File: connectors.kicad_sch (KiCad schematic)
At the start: 21 parts, among them J2 52746-1271, J4 SS5-10-3.00-L-D-K-TR, J8 2, M1 MountingHole_Pad, M2 MountingHole_Pad, M3 MountingHole_Pad, M4 MountingHole_Pad, U13 TXB0104RUT, U2 TXB0104RUT

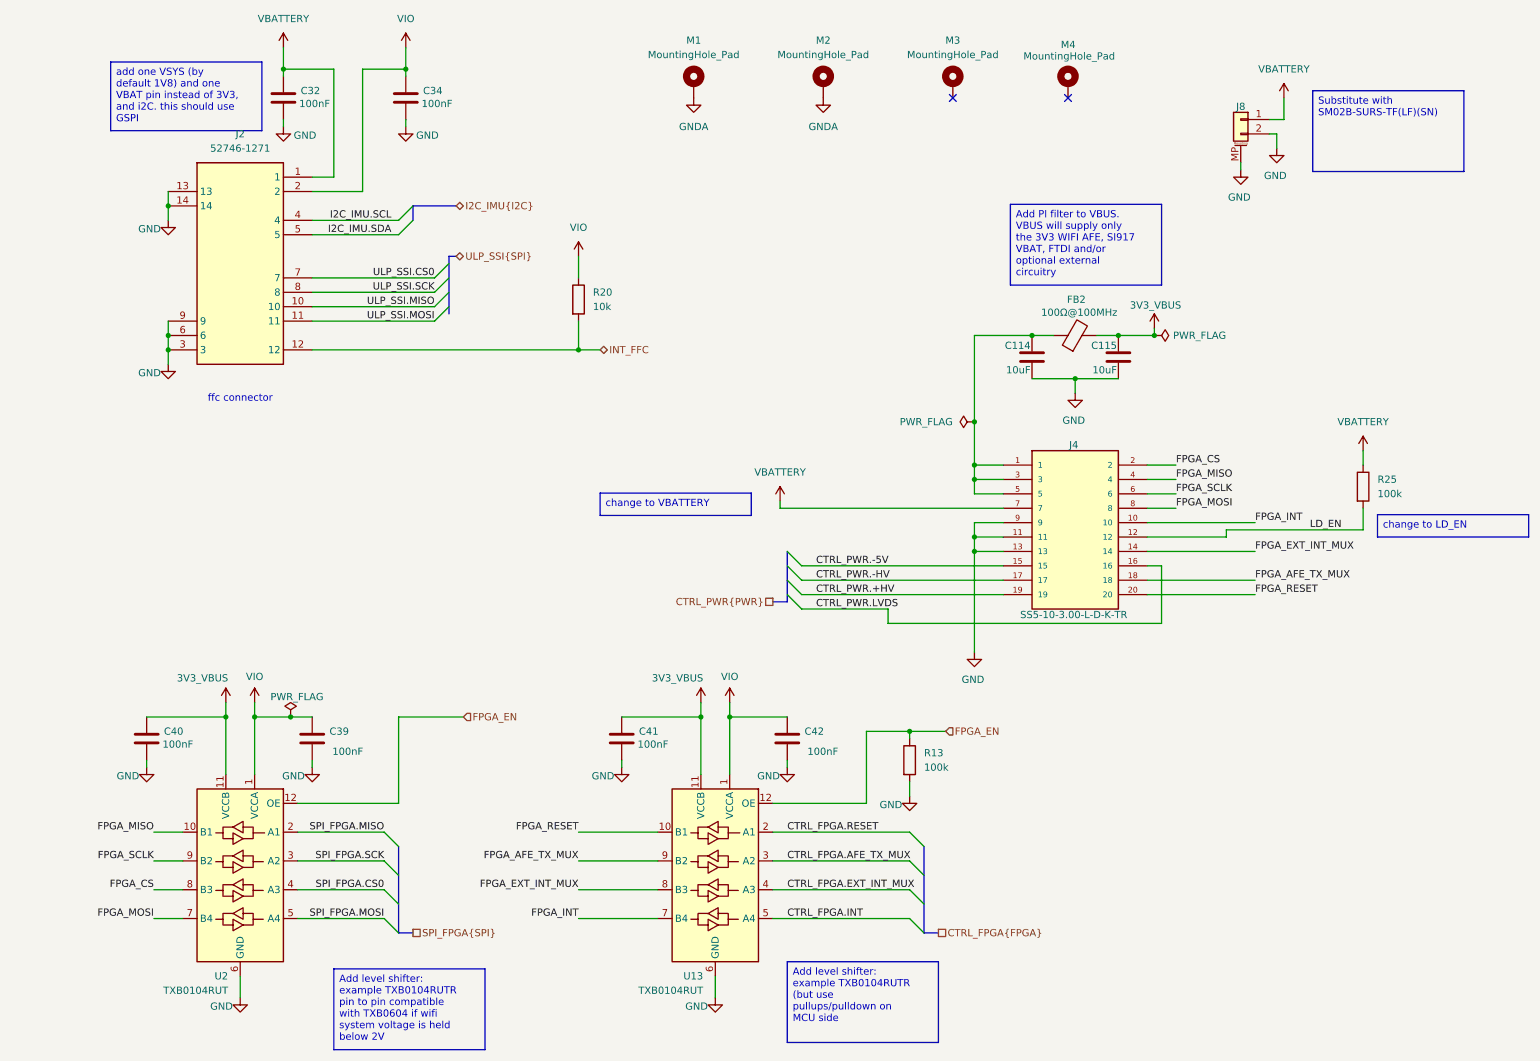
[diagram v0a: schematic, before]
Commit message: new debug connector SOICbite, new board shape, new placement, addition of 22 ohm resistance in fast digital signals as spi
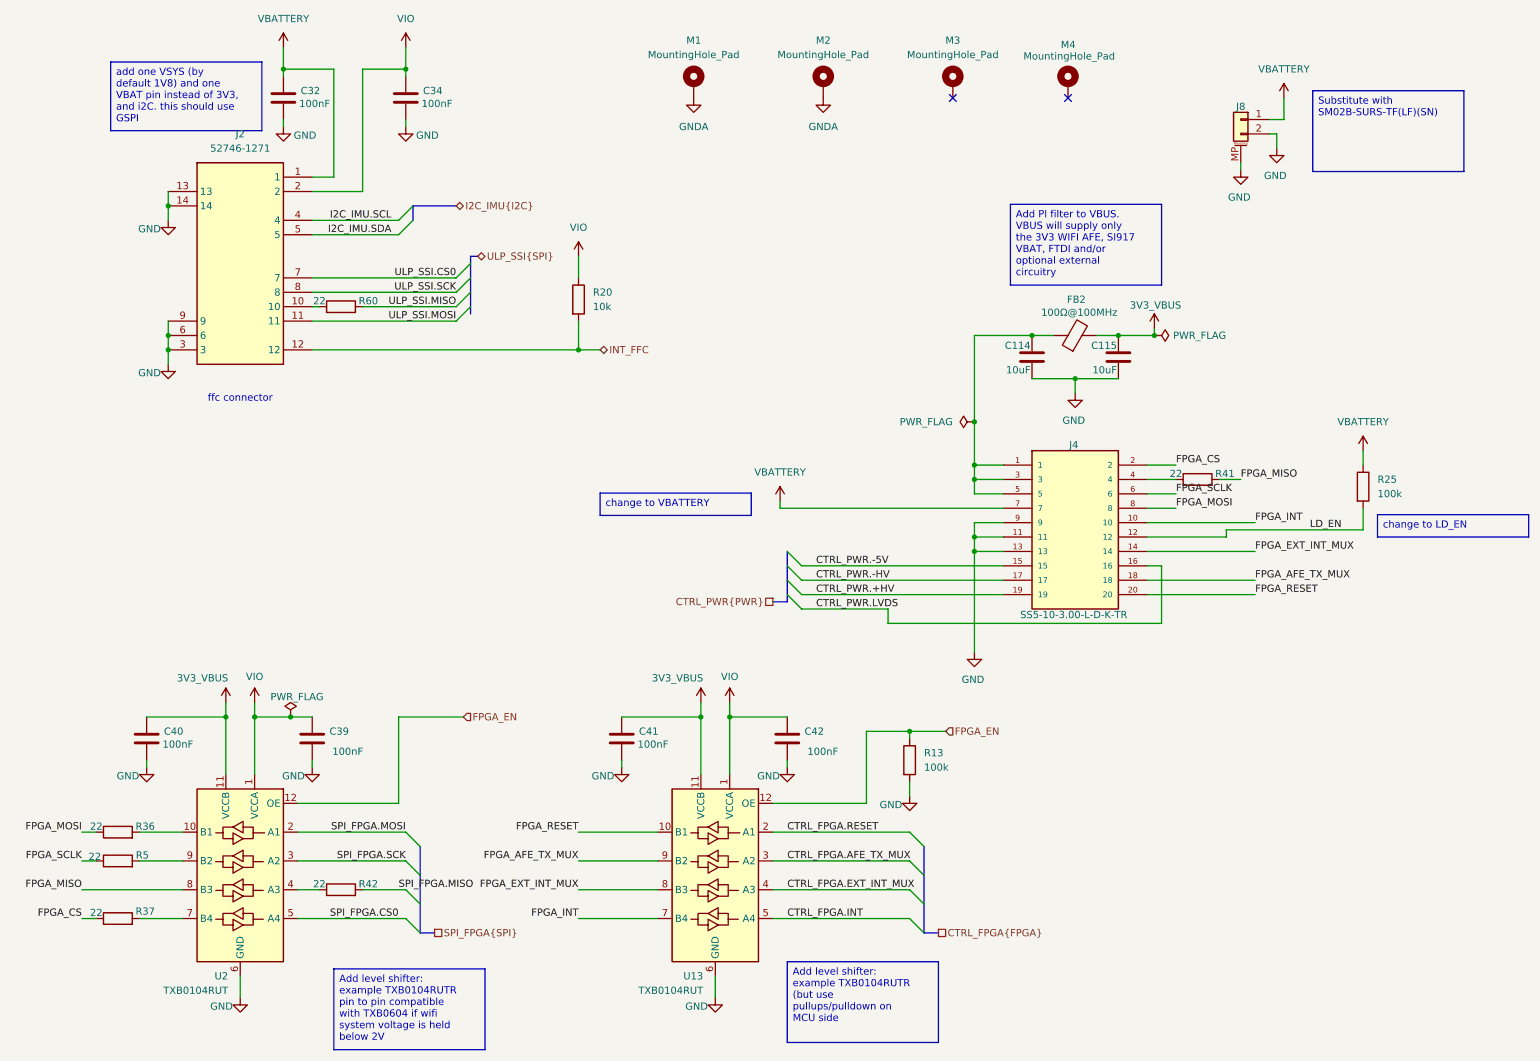
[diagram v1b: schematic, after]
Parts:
- added R36, R37, R41, R42, R5, R60: 22, Resistor_SMD:R_0201_0603Metric, symbol #dzdb:g_res/R-22-0201
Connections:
- net FPGA_CS: now also R37.1; no longer U2.8 (B3)
- net FPGA_MISO: now also U2.8 (B3), R41.2; no longer J4.4, U2.10 (B1)
- net FPGA_MOSI: now also R36.1; no longer U2.7 (B4)
- net FPGA_SCLK: now also R5.1; no longer U2.9 (B2)
- net SPI_FPGA.CS0: now also U2.5 (A4); no longer U2.4 (A3)
- net SPI_FPGA.MISO: now also R42.2; no longer U2.2 (A1)
- net SPI_FPGA.MOSI: now also U2.2 (A1); no longer U2.5 (A4)
- net ULP_SSI.MISO: now also R60.2; no longer J2.10
- new net: J4.4, R41.1
- new net: R36.2, U2.10 (B1)
- new net: R42.1, U2.4 (A3)
- new net: R37.2, U2.7 (B4)
- new net: R5.2, U2.9 (B2)
- new net: J2.10, R60.1

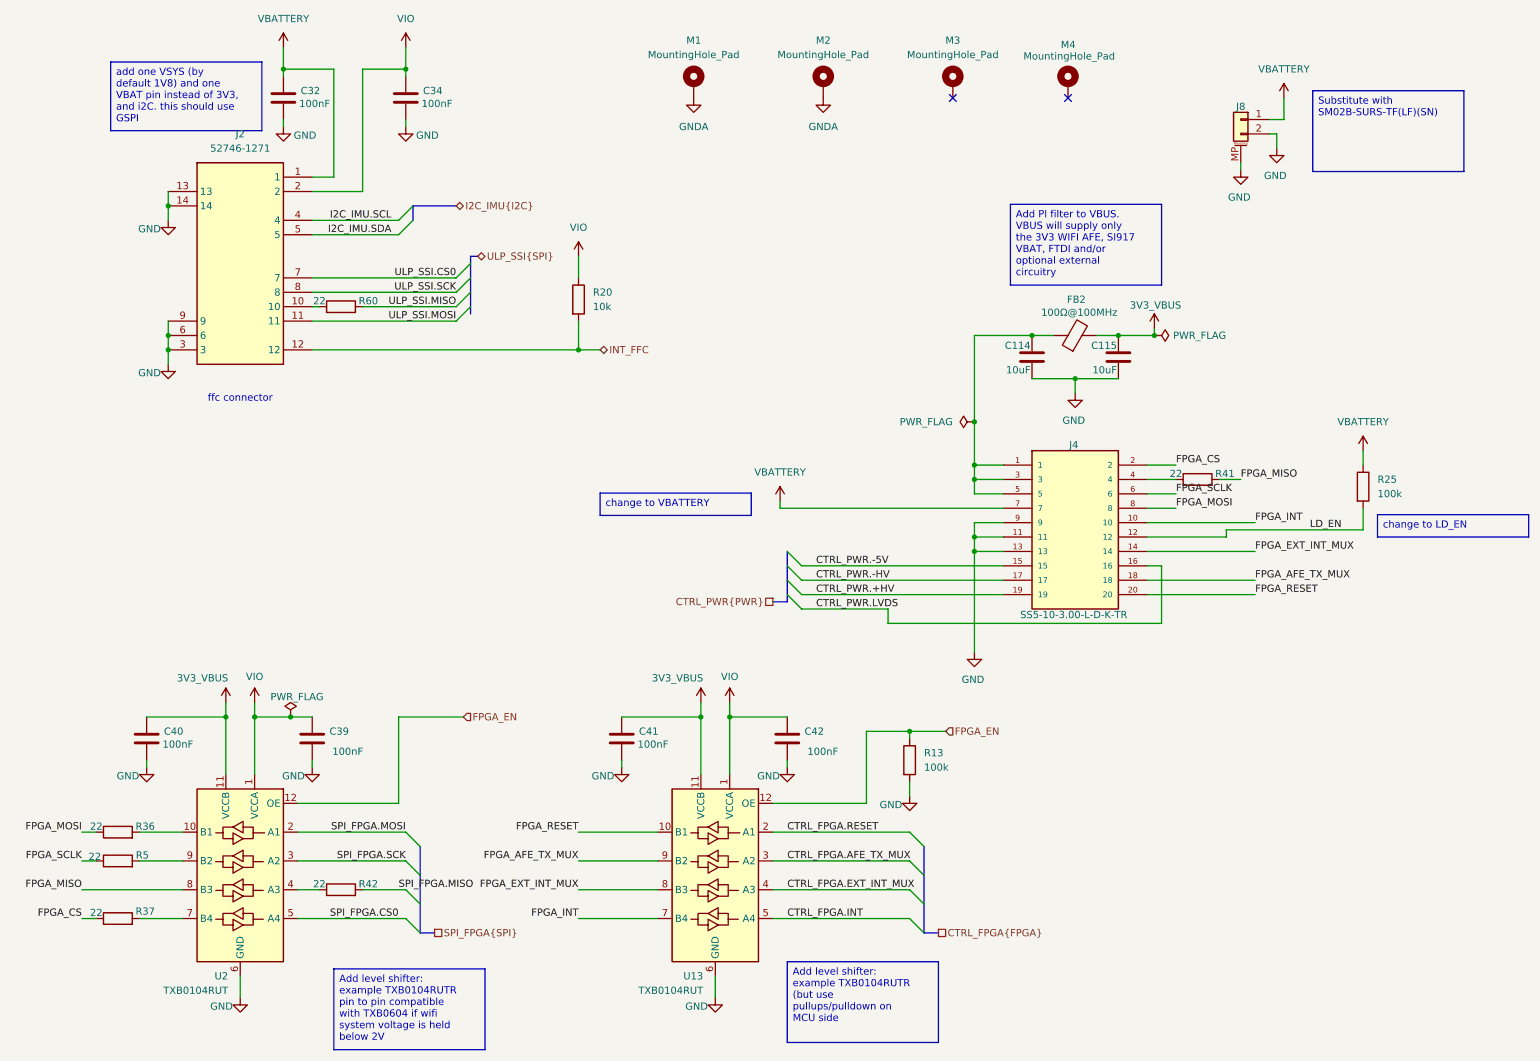
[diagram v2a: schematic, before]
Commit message: updated routing SPI, change 0402 to 0201
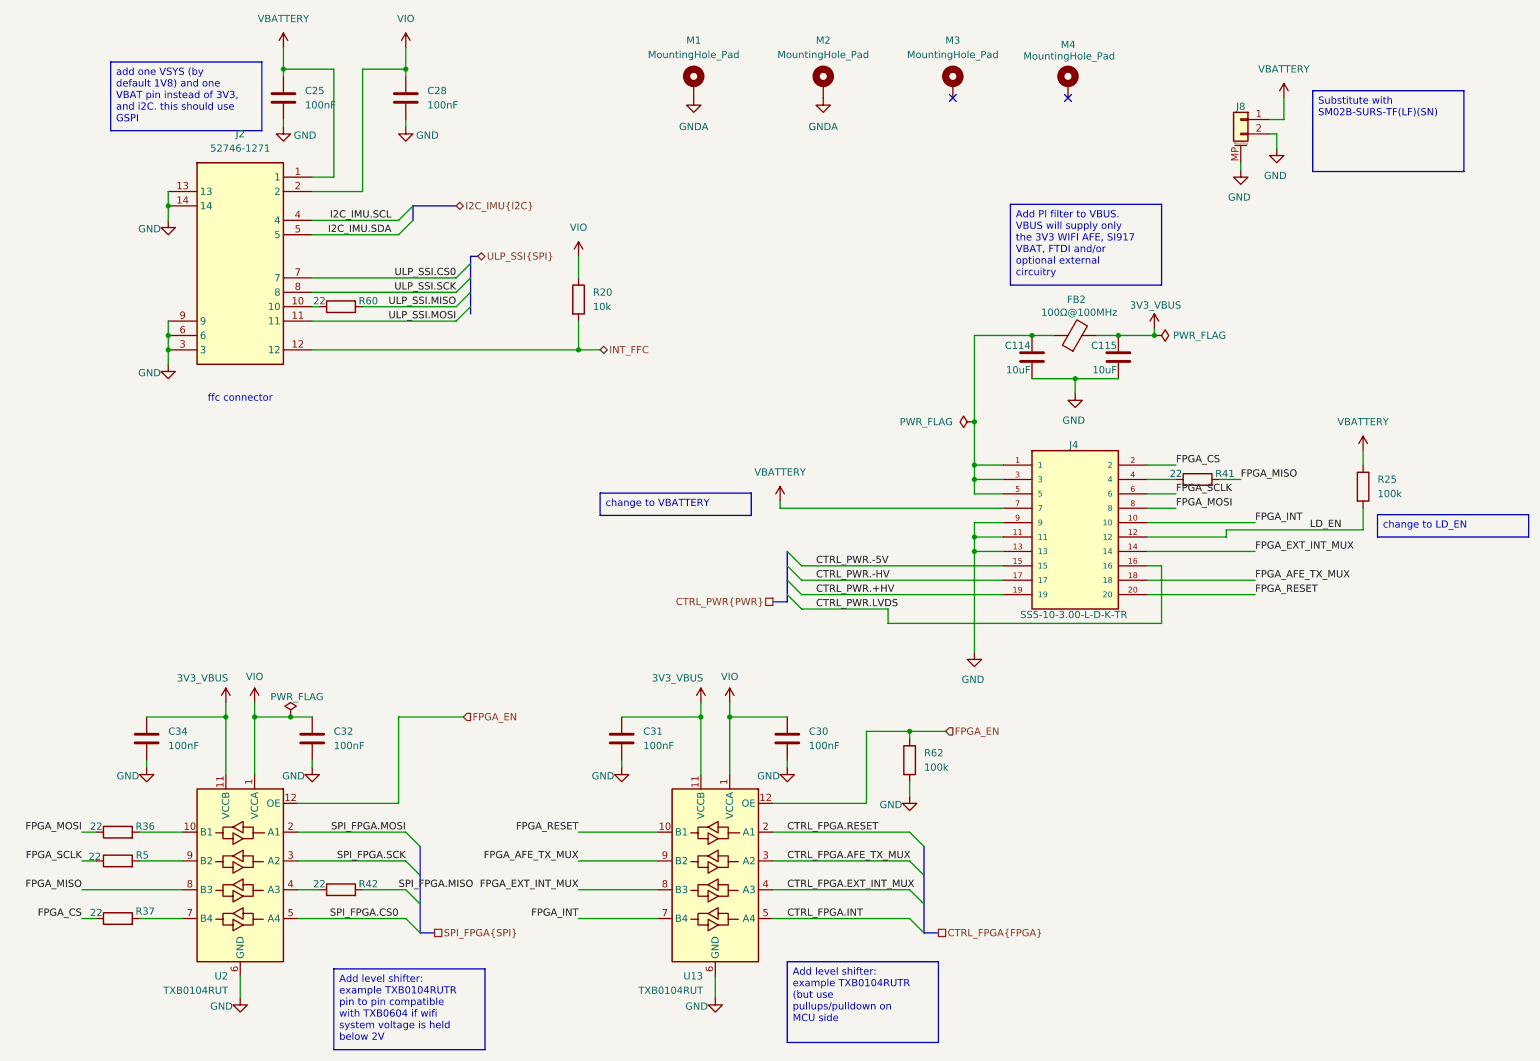
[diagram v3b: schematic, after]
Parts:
- removed C32, C34, C39, C40, C41, C42: 100nF, Capacitor_SMD:C_0603_1608Metric, symbol #dzdb:g_cap/C-100n-0603
- removed R13: 100k, Resistor_SMD:R_0402_1005Metric, symbol #dzdb:g_res/R-100k-0402
- removed R20: 10k, Resistor_SMD:R_0402_1005Metric, symbol #dzdb:g_res/R-10k-0402
- added C25, C28, C30, C31, C32, C34: 100nF, Capacitor_SMD:C_0201_0603Metric, symbol #dzdb:g_cap/C-100n-0201
- added R20: 10k, Resistor_SMD:R_0201_0603Metric, symbol #dzdb:g_res/R-10K-0201
- added R62: 100k, Resistor_SMD:R_0201_0603Metric, symbol #dzdb:g_res/R-100K-0201
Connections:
- net 3V3_VBUS: now also C31.1, C34.1
- net FPGA_EN: now also R62.1
- net GND: now also C25.2, C28.2, C30.2, C31.2, C32.2, C34.2, R62.2
- net INT_FFC: now also R20.2
- net VBATTERY: now also C25.1
- net VIO: now also C28.1, C30.1, C32.1, R20.1

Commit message: updated routing
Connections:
- net GNDA is gone; now on net GND: M1.1, M2.1
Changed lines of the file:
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@@
 			)
 		)
-		(property "Value" "GNDA"
-			(at 151.13 34.29 0)
+		(property "Value" "GND"
+			(at 153.67 30.4799 0)
 			(show_name no)
 			(do_not_autoplace no)
@@
 					(size 1.27 1.27)
 				)
+				(justify left)
 			)
 		)
@@
 			)
 		)
-		(property "Value" "GNDA"
-			(at 128.27 34.29 0)
+		(property "Value" "GND"
+			(at 130.81 30.4799 0)
 			(show_name no)
 			(do_not_autoplace no)
@@
 					(size 1.27 1.27)
 				)
+				(justify left)
 			)
 		)
